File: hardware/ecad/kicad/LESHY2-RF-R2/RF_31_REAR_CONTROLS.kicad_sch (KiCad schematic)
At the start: 14 parts, among them SW3 Alps Alpine EC11E18244AU, SW4 OMRON B3S-1100P, U100 TCA6424ARGJR, U98 Texas Instruments TPD4E05U06D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, U99 Texas Instruments TPD4E05U06D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

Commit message: Verify factory-placeable Airband filter
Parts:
- renumbered C250 to C249, C251 to C250, C252 to C251, C253 to C252
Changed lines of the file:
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@@
 		(on_board yes)
 		(dnp no)
-		(property "Reference" "C250"
+		(property "Reference" "C249"
 			(at 55.88 44.45 0)
 			(show_name no)
@@
 			(project "LESHY2-RF-R2"
 				(path "/144a8f7c-debe-52f6-a7eb-eadc6d3faec6"
-					(reference "C250")
+					(reference "C249")
 					(unit 1)
 				)
@@
 		(on_board yes)
 		(dnp no)
-		(property "Reference" "C251"
+		(property "Reference" "C250"
 			(at 147.32 44.45 0)
 			(show_name no)
@@
 			(project "LESHY2-RF-R2"
 				(path "/144a8f7c-debe-52f6-a7eb-eadc6d3faec6"
-					(reference "C251")
+					(reference "C250")
 					(unit 1)
 				)
@@
 		(on_board yes)
 		(dnp no)
-		(property "Reference" "C252"
+		(property "Reference" "C251"
 			(at 238.76 44.45 0)
 			(show_name no)
@@
 			(project "LESHY2-RF-R2"
 				(path "/144a8f7c-debe-52f6-a7eb-eadc6d3faec6"
-					(reference "C252")
+					(reference "C251")
 					(unit 1)
 				)
@@
 		(on_board yes)
 		(dnp no)
-		(property "Reference" "C253"
+		(property "Reference" "C252"
 			(at 330.20 44.45 0)
 			(show_name no)
@@
 			(project "LESHY2-RF-R2"
 				(path "/144a8f7c-debe-52f6-a7eb-eadc6d3faec6"
-					(reference "C253")
-					(unit 1)
-				)
+					(reference "C252")
+					(unit 1)
+				)

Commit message: Complete current R2 schematic and sourcing revalidation
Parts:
- renumbered C249 to C258, C250 to C259, C251 to C260, C252 to C261, R235 to R244, R236 to R245, R237 to R246, R238 to R247, R239 to R248, U98 to U104, U99 to U105, U100 to U106
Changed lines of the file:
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@@
 		(on_board yes)
 		(dnp no)
-		(property "Reference" "C249"
+		(property "Reference" "C258"
 			(at 55.88 44.45 0)
 			(show_name no)
@@
 			(project "LESHY2-RF-R2"
 				(path "/144a8f7c-debe-52f6-a7eb-eadc6d3faec6"
-					(reference "C249")
+					(reference "C258")
 					(unit 1)
 				)
@@
 		(on_board yes)
 		(dnp no)
-		(property "Reference" "C250"
+		(property "Reference" "C259"
 			(at 147.32 44.45 0)
 			(show_name no)
@@
 			(project "LESHY2-RF-R2"
 				(path "/144a8f7c-debe-52f6-a7eb-eadc6d3faec6"
-					(reference "C250")
+					(reference "C259")
 					(unit 1)
 				)
@@
 		(on_board yes)
 		(dnp no)
-		(property "Reference" "C251"
+		(property "Reference" "C260"
 			(at 238.76 44.45 0)
 			(show_name no)
@@
 			(project "LESHY2-RF-R2"
 				(path "/144a8f7c-debe-52f6-a7eb-eadc6d3faec6"
-					(reference "C251")
+					(reference "C260")
 					(unit 1)
 				)
@@
 		(on_board yes)
 		(dnp no)
-		(property "Reference" "C252"
+		(property "Reference" "C261"
 			(at 330.20 44.45 0)
 			(show_name no)
@@
 			(project "LESHY2-RF-R2"
 				(path "/144a8f7c-debe-52f6-a7eb-eadc6d3faec6"
-					(reference "C252")
+					(reference "C261")
 					(unit 1)
 				)
@@
 		(on_board yes)
 		(dnp no)
-		(property "Reference" "R235"
+		(property "Reference" "R244"
 			(at 421.64 44.45 0)
 			(show_name no)
@@
 			(project "LESHY2-RF-R2"
 				(path "/144a8f7c-debe-52f6-a7eb-eadc6d3faec6"
-					(reference "R235")
+					(reference "R244")
 					(unit 1)
 				)
@@
 		(on_board yes)
 		(dnp no)
-		(property "Reference" "R236"
+		(property "Reference" "R245"
 			(at 513.08 44.45 0)
 			(show_name no)
@@
 			(project "LESHY2-RF-R2"
 				(path "/144a8f7c-debe-52f6-a7eb-eadc6d3faec6"
-					(reference "R236")
+					(reference "R245")
 					(unit 1)
 				)
@@
 		(on_board yes)
 		(dnp no)
-		(property "Reference" "R237"
+		(property "Reference" "R246"
 			(at 604.52 44.45 0)
 			(show_name no)
@@
 			(project "LESHY2-RF-R2"
 				(path "/144a8f7c-debe-52f6-a7eb-eadc6d3faec6"
-					(reference "R237")
+					(reference "R246")
 					(unit 1)
 				)
@@
 		(on_board yes)
 		(dnp no)
-		(property "Reference" "R238"
+		(property "Reference" "R247"
 			(at 695.96 44.45 0)
 			(show_name no)
@@
 			(project "LESHY2-RF-R2"
 				(path "/144a8f7c-debe-52f6-a7eb-eadc6d3faec6"
-					(reference "R238")
+					(reference "R247")
 					(unit 1)
 				)
@@
 		(on_board yes)
 		(dnp no)
-		(property "Reference" "R239"
+		(property "Reference" "R248"
 			(at 787.40 44.45 0)
 			(show_name no)
@@
 			(project "LESHY2-RF-R2"
 				(path "/144a8f7c-debe-52f6-a7eb-eadc6d3faec6"
-					(reference "R239")
+					(reference "R248")
 					(unit 1)
 				)
@@
 		(on_board yes)
 		(dnp no)
-		(property "Reference" "U98"
+		(property "Reference" "U104"
 			(at 1061.72 44.45 0)
 			(show_name no)
@@
 			(project "LESHY2-RF-R2"
 				(path "/144a8f7c-debe-52f6-a7eb-eadc6d3faec6"
-					(reference "U98")
+					(reference "U104")
 					(unit 1)
 				)
@@
 		(on_board yes)
 		(dnp no)
-		(property "Reference" "U99"
+		(property "Reference" "U105"
 			(at 55.88 80.01 0)
 			(show_name no)
@@
 			(project "LESHY2-RF-R2"
 				(path "/144a8f7c-debe-52f6-a7eb-eadc6d3faec6"
-					(reference "U99")
+					(reference "U105")
 					(unit 1)
 				)
@@
 		(on_board yes)
 		(dnp no)
-		(property "Reference" "U100"
+		(property "Reference" "U106"
 			(at 147.32 80.01 0)
 			(show_name no)
@@
 			(project "LESHY2-RF-R2"
 				(path "/144a8f7c-debe-52f6-a7eb-eadc6d3faec6"
-					(reference "U100")
-					(unit 1)
-				)
+					(reference "U106")
+					(unit 1)
+				)

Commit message: Canonicalize physical ground anchors
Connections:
- net ENCODER_PTT_ESD_GROUND is gone; now on net POWER_GROUND: U104.3 (GND_3), U104.8 (GND_8)
- net REAR_CONTROL_ESD_GROUND is gone; now on net POWER_GROUND: U105.3 (GND_3), U105.8 (GND_8)
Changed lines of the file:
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@@
 		(effects (font (size 1.27 1.27)))
 	)
-	(label "ENCODER_PTT_ESD_GROUND"
+	(label "POWER_GROUND"
 		(at 1041.40 53.34 0)
 		(effects (font (size 1.27 1.27)))
@@
 	(no_connect (at 1082.04 50.80)
 	)
-	(label "ENCODER_PTT_ESD_GROUND"
+	(label "POWER_GROUND"
 		(at 1082.04 53.34 180)
 		(effects (font (size 1.27 1.27)) (justify right bottom))
@@
 	(no_connect (at 35.56 86.36)
 	)
-	(label "REAR_CONTROL_ESD_GROUND"
+	(label "POWER_GROUND"
 		(at 35.56 88.90 0)
 		(effects (font (size 1.27 1.27)))
@@
 	(no_connect (at 76.20 86.36)
 	)
-	(label "REAR_CONTROL_ESD_GROUND"
+	(label "POWER_GROUND"
 		(at 76.20 88.90 180)
 		(effects (font (size 1.27 1.27)) (justify right bottom))

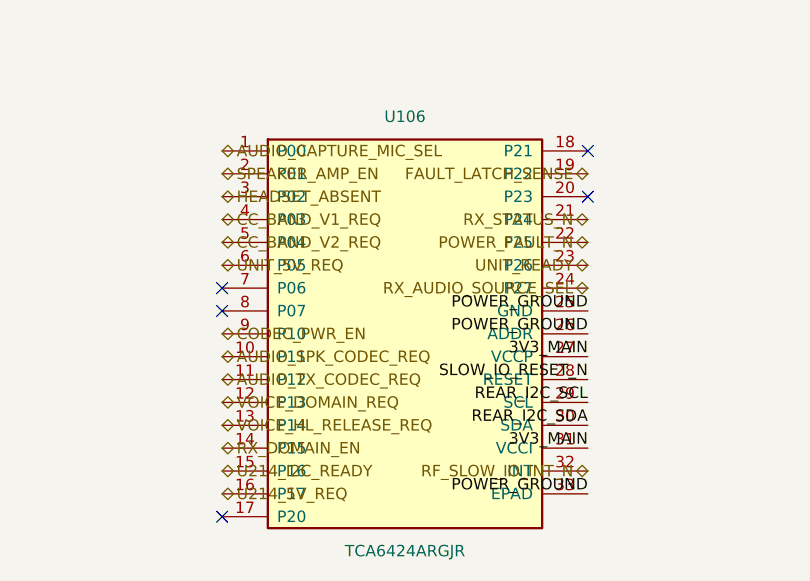
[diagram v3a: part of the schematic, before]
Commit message: Route safety control slice
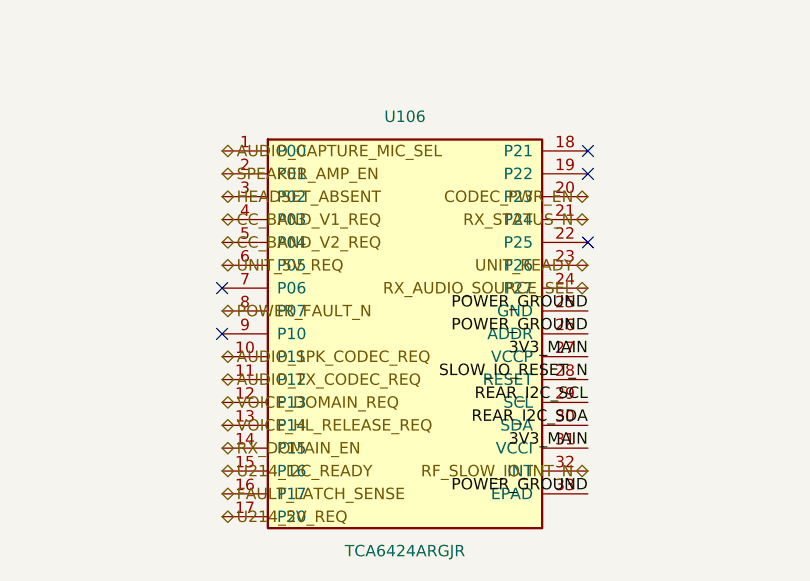
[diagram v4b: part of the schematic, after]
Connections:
- net CODEC_PWR_EN: now also U106.20 (P23); no longer U106.9 (P10)
- net FAULT_LATCH_SENSE: now also U106.16 (P17); no longer U106.19 (P22)
- net POWER_FAULT_N: now also U106.8 (P07); no longer U106.22 (P25)
- net U214_5V_REQ: now also U106.17 (P20); no longer U106.16 (P17)
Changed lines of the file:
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@@
 	(no_connect (at 127.00 99.06)
 	)
-	(no_connect (at 127.00 101.60)
+	(hierarchical_label "POWER_FAULT_N"
+		(shape bidirectional)
+		(at 127.00 101.60 0)
+		(effects (font (size 1.27 1.27)))
 	)
-	(hierarchical_label "CODEC_PWR_EN"
-		(shape bidirectional)
-		(at 127.00 104.14 0)
-		(effects (font (size 1.27 1.27)))
+	(no_connect (at 127.00 104.14)
 	)
 	(hierarchical_label "AUDIO_SPK_CODEC_REQ"
@@
 		(effects (font (size 1.27 1.27)))
 	)
-	(hierarchical_label "U214_5V_REQ"
+	(hierarchical_label "FAULT_LATCH_SENSE"
 		(shape bidirectional)
 		(at 127.00 121.92 0)
 		(effects (font (size 1.27 1.27)))
 	)
-	(no_connect (at 127.00 124.46)
+	(hierarchical_label "U214_5V_REQ"
+		(shape bidirectional)
+		(at 127.00 124.46 0)
+		(effects (font (size 1.27 1.27)))
 	)
 	(no_connect (at 167.64 83.82)
 	)
-	(hierarchical_label "FAULT_LATCH_SENSE"
+	(no_connect (at 167.64 86.36)
+	)
+	(hierarchical_label "CODEC_PWR_EN"
 		(shape bidirectional)
-		(at 167.64 86.36 180)
+		(at 167.64 88.90 180)
 		(effects (font (size 1.27 1.27)) (justify right bottom))
-	)
-	(no_connect (at 167.64 88.90)
 	)
 	(hierarchical_label "RX_STATUS_N"
@@
 		(effects (font (size 1.27 1.27)) (justify right bottom))
 	)
-	(hierarchical_label "POWER_FAULT_N"
-		(shape bidirectional)
-		(at 167.64 93.98 180)
-		(effects (font (size 1.27 1.27)) (justify right bottom))
+	(no_connect (at 167.64 93.98)
 	)
 	(hierarchical_label "UNIT_READY"

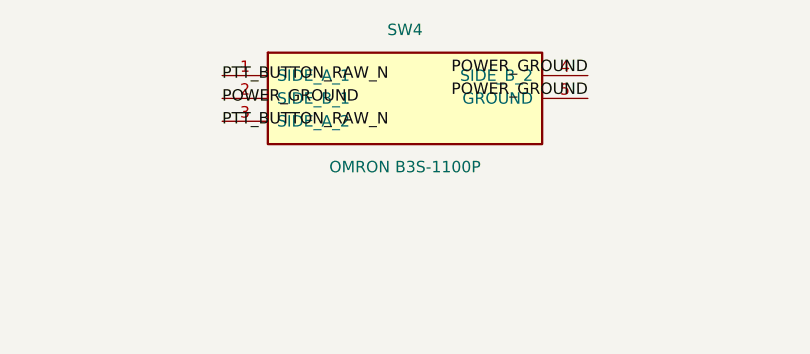
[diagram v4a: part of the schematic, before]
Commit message: Correct exact connector and protection geometry; expand electrical review
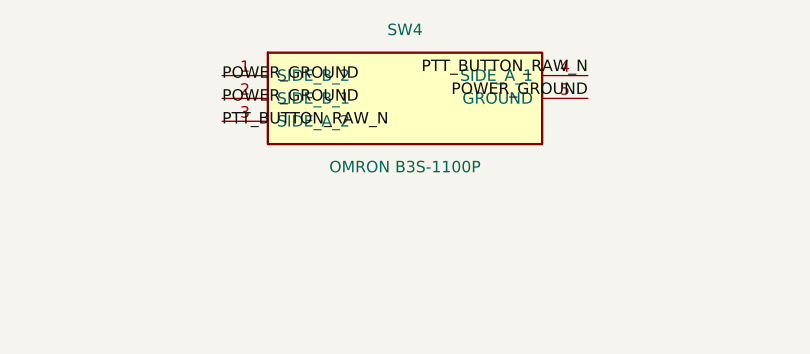
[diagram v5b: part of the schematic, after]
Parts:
- SW4: footprint Leshy2:B3S-1100P -> Leshy2_R2:B3S-1100P
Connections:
- net POWER_GROUND: now also SW4.1 (SIDE_B_2); no longer SW4.4 (SIDE_B_2)
- net PTT_BUTTON_RAW_N: now also SW4.4 (SIDE_A_1); no longer SW4.1 (SIDE_A_1)
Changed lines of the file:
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@@
 			(effects (font (size 1.27 1.27)))
 		)
-		(property "Footprint" "Leshy2:B3S-1100P"
+		(property "Footprint" "Leshy2_R2:B3S-1100P"
 			(at 970.28 52.07 0)
 			(show_name no)
@@
 		)
 	)
-	(label "PTT_BUTTON_RAW_N"
+	(label "POWER_GROUND"
 		(at 949.96 49.53 0)
 		(effects (font (size 1.27 1.27)))
@@
 		(effects (font (size 1.27 1.27)))
 	)
-	(label "POWER_GROUND"
+	(label "PTT_BUTTON_RAW_N"
 		(at 990.60 49.53 180)
 		(effects (font (size 1.27 1.27)) (justify right bottom))

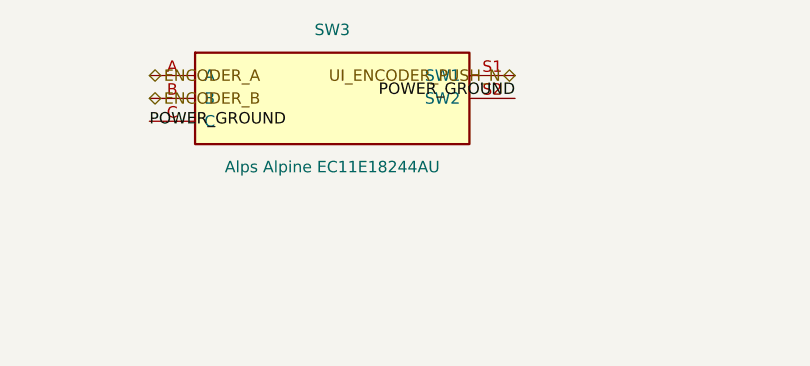
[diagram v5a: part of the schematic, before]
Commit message: Correct EC11 fit and add seven reviewed LED routes
Integrate the exact-axis engineering EC11 footprint and local support placement while preserving all765 RF copper objects and five encoder world pad/net pairs. Add51 UI segments and8 vias for seven reviewed anode nets, retaining all33 prior UI copper objects and excluding FAULT.

Refresh native DRC, four-face component views, routing counters, H3 contract hashes, typed ERC and source-path triage. Correct stale holder/JAE evidence wording; retain24 raw ERC findings, open mechanical/power gates and historical firmware qualification. Add actual-files freshness and public-counter regressions.

Checks:1182 hardware tests with46 skips;116 native focused tests without skips; both boards DRC0 violations/0 schematic-parity findings;115 routes,682 segments,175 vias,197 resolved,3071 remaining. No new MPN, order or fabrication authorization.
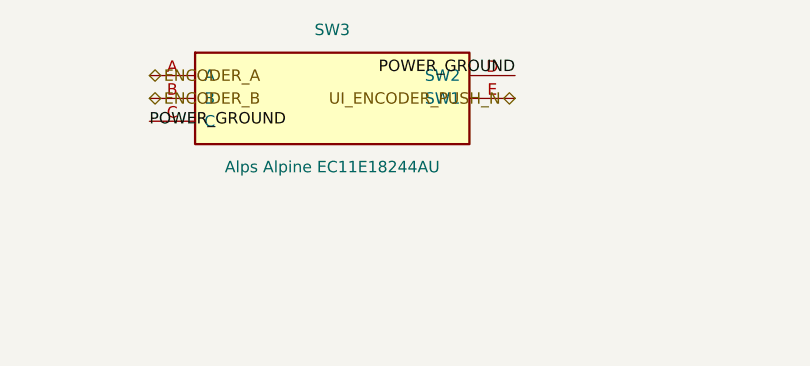
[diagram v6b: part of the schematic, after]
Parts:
- SW3: footprint Rotary_Encoder:RotaryEncoder_Alps_EC11E-Switch_Vertical_H20mm_MountingHoles -> Leshy2_R2:EC11E18244AU-ENGINEERING-PTH
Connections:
- net POWER_GROUND: now also SW3.D (SW2); no longer SW3.S2 (SW2)
- net UI_ENCODER_PUSH_N: now also SW3.E (SW1); no longer SW3.S1 (SW1)
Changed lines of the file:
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@@
 			(effects (font (size 1.27 1.27)))
 		)
-		(property "Footprint" "Rotary_Encoder:RotaryEncoder_Alps_EC11E-Switch_Vertical_H20mm_MountingHoles"
+		(property "Footprint" "Leshy2_R2:EC11E18244AU-ENGINEERING-PTH"
 			(at 878.84 52.07 0)
 			(show_name no)
@@
 		(pin "C"
 		)
-		(pin "S1"
+		(pin "D"
 		)
-		(pin "S2"
+		(pin "E"
 		)
 		(instances
@@
 		(effects (font (size 1.27 1.27)))
 	)
-	(hierarchical_label "UI_ENCODER_PUSH_N"
-		(shape bidirectional)
+	(label "POWER_GROUND"
 		(at 899.16 49.53 180)
 		(effects (font (size 1.27 1.27)) (justify right bottom))
 	)
-	(label "POWER_GROUND"
+	(hierarchical_label "UI_ENCODER_PUSH_N"
+		(shape bidirectional)
 		(at 899.16 52.07 180)
 		(effects (font (size 1.27 1.27)) (justify right bottom))
